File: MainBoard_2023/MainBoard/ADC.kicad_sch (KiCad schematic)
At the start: 6 parts

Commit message: ERC通った
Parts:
- added J12, J13, J14: Conn_01x03, symbol Connector_Generic:Conn_01x03
- gave numbers to parts that had none: 6
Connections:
- net +3.3V: now also J12.1 (Pin_1), J13.1 (Pin_1), J14.1 (Pin_1)
- net GND: now also J12.2 (Pin_2), J13.2 (Pin_2), J14.2 (Pin_2)
- net at IC2.10 (AIN1): now also J14.3 (Pin_3)
- net at IC2.6 (AIN3/REFN1): now also J12.3 (Pin_3)
- net at IC2.7 (AIN2): now also J13.3 (Pin_3)

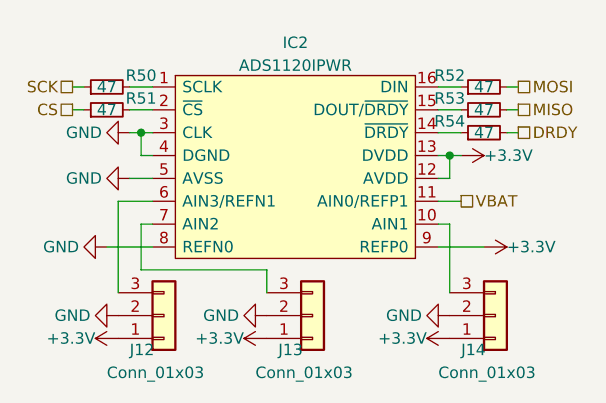
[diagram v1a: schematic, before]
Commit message: フットプリントをすべて割り当て
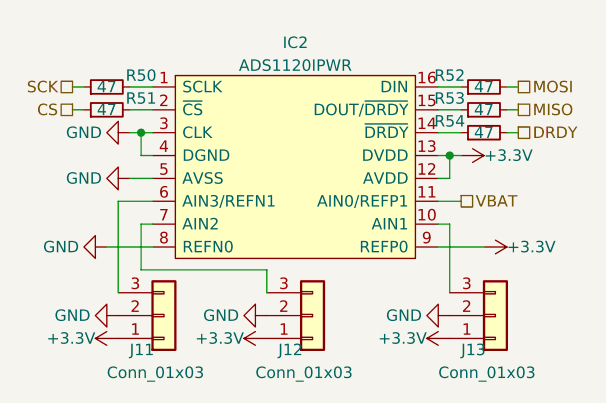
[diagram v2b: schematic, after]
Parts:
- IC2: footprint SOP65P640X120-16N -> ADS1120IPWR:ADS1120IPWR
- J11: renamed from J12; footprint (none) -> B03B-PASK-1:B03B-PASK-1
- J12: renamed from J13; footprint (none) -> B03B-PASK-1:B03B-PASK-1
- J13: renamed from J14; footprint (none) -> B03B-PASK-1:B03B-PASK-1
- R50, R51, R52, R53, R54: footprint (none) -> Resistor_SMD:R_0603_1608Metric_Pad0.98x0.95mm_HandSolder
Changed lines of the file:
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@@
   (symbol (lib_id "Connector_Generic:Conn_01x03") (at 166.37 110.49 0) (mirror x) (unit 1)
     (in_bom yes) (on_board yes)
-    (property "Reference" "J14" (id 0) (at 162.56 114.3 0)
+    (property "Reference" "J13" (id 0) (at 162.56 114.3 0)
       (effects (font (size 1.27 1.27)) (justify left))
     )
@@
       (effects (font (size 1.27 1.27)) (justify left))
     )
-    (property "Footprint" "" (id 2) (at 166.37 110.49 0)
+    (property "Footprint" "B03B-PASK-1:B03B-PASK-1" (id 2) (at 166.37 110.49 0)
       (effects (font (size 1.27 1.27)) hide)
     )
@@
   (symbol (lib_id "power:+3.3V") (at 165.1 102.87 270) (unit 1)
     (in_bom yes) (on_board yes)
-    (property "Reference" "#PWR0121" (id 0) (at 161.29 102.87 0)
+    (property "Reference" "#PWR0122" (id 0) (at 161.29 102.87 0)
       (effects (font (size 1.27 1.27)) hide)
     )
@@
     (property "Reference" "R53" (id 0) (at 161.29 86.36 90))
     (property "Value" "47" (id 1) (at 165.1 87.63 90))
-    (property "Footprint" "" (id 2) (at 165.1 87.63 0)
+    (property "Footprint" "Resistor_SMD:R_0603_1608Metric_Pad0.98x0.95mm_HandSolder" (id 2) (at 165.1 87.63 0)
       (effects (font (size 1.27 1.27)) hide)
     )
@@
   (symbol (lib_id "Connector_Generic:Conn_01x03") (at 146.05 110.49 0) (mirror x) (unit 1)
     (in_bom yes) (on_board yes)
-    (property "Reference" "J13" (id 0) (at 142.24 114.3 0)
+    (property "Reference" "J12" (id 0) (at 142.24 114.3 0)
       (effects (font (size 1.27 1.27)) (justify left))
     )
@@
       (effects (font (size 1.27 1.27)) (justify left))
     )
-    (property "Footprint" "" (id 2) (at 146.05 110.49 0)
+    (property "Footprint" "B03B-PASK-1:B03B-PASK-1" (id 2) (at 146.05 110.49 0)
       (effects (font (size 1.27 1.27)) hide)
     )
@@
     (property "Reference" "R51" (id 0) (at 127 86.36 90))
     (property "Value" "47" (id 1) (at 123.19 87.63 90))
-    (property "Footprint" "" (id 2) (at 123.19 87.63 0)
+    (property "Footprint" "Resistor_SMD:R_0603_1608Metric_Pad0.98x0.95mm_HandSolder" (id 2) (at 123.19 87.63 0)
       (effects (font (size 1.27 1.27)) hide)
     )
@@
   (symbol (lib_id "power:GND") (at 161.29 110.49 270) (unit 1)
     (in_bom yes) (on_board yes)
-    (property "Reference" "#PWR0118" (id 0) (at 154.94 110.49 0)
+    (property "Reference" "#PWR0119" (id 0) (at 154.94 110.49 0)
       (effects (font (size 1.27 1.27)) hide)
     )
@@
     (property "Reference" "R50" (id 0) (at 127 83.82 90))
     (property "Value" "47" (id 1) (at 123.19 85.09 90))
-    (property "Footprint" "" (id 2) (at 123.19 85.09 0)
+    (property "Footprint" "Resistor_SMD:R_0603_1608Metric_Pad0.98x0.95mm_HandSolder" (id 2) (at 123.19 85.09 0)
       (effects (font (size 1.27 1.27)) hide)
     )
@@
     (property "Reference" "R54" (id 0) (at 161.29 88.9 90))
     (property "Value" "47" (id 1) (at 165.1 90.17 90))
-    (property "Footprint" "" (id 2) (at 165.1 90.17 0)
+    (property "Footprint" "Resistor_SMD:R_0603_1608Metric_Pad0.98x0.95mm_HandSolder" (id 2) (at 165.1 90.17 0)
       (effects (font (size 1.27 1.27)) hide)
     )
@@
     (property "Reference" "R52" (id 0) (at 161.29 83.82 90))
     (property "Value" "47" (id 1) (at 165.1 85.09 90))
-    (property "Footprint" "" (id 2) (at 165.1 85.09 0)
+    (property "Footprint" "Resistor_SMD:R_0603_1608Metric_Pad0.98x0.95mm_HandSolder" (id 2) (at 165.1 85.09 0)
       (effects (font (size 1.27 1.27)) hide)
     )
@@
   (symbol (lib_id "power:GND") (at 125.73 95.25 270) (unit 1)
     (in_bom yes) (on_board yes)
-    (property "Reference" "#PWR0115" (id 0) (at 119.38 95.25 0)
+    (property "Reference" "#PWR0116" (id 0) (at 119.38 95.25 0)
       (effects (font (size 1.27 1.27)) hide)
     )
@@
   (symbol (lib_id "power:+3.3V") (at 140.97 113.03 90) (mirror x) (unit 1)
     (in_bom yes) (on_board yes)
-    (property "Reference" "#PWR0117" (id 0) (at 144.78 113.03 0)
+    (property "Reference" "#PWR0118" (id 0) (at 144.78 113.03 0)
       (effects (font (size 1.27 1.27)) hide)
     )
@@
   (symbol (lib_id "power:GND") (at 124.46 110.49 270) (unit 1)
     (in_bom yes) (on_board yes)
-    (property "Reference" "#PWR0112" (id 0) (at 118.11 110.49 0)
+    (property "Reference" "#PWR0113" (id 0) (at 118.11 110.49 0)
       (effects (font (size 1.27 1.27)) hide)
     )
@@
   (symbol (lib_id "power:GND") (at 123.19 102.87 270) (unit 1)
     (in_bom yes) (on_board yes)
-    (property "Reference" "#PWR0111" (id 0) (at 116.84 102.87 0)
+    (property "Reference" "#PWR0112" (id 0) (at 116.84 102.87 0)
       (effects (font (size 1.27 1.27)) hide)
     )
@@
   (symbol (lib_id "power:+3.3V") (at 124.46 113.03 90) (mirror x) (unit 1)
     (in_bom yes) (on_board yes)
-    (property "Reference" "#PWR0113" (id 0) (at 128.27 113.03 0)
+    (property "Reference" "#PWR0114" (id 0) (at 128.27 113.03 0)
       (effects (font (size 1.27 1.27)) hide)
     )
@@
   (symbol (lib_id "power:+3.3V") (at 162.56 92.71 270) (unit 1)
     (in_bom yes) (on_board yes)
-    (property "Reference" "#PWR0120" (id 0) (at 158.75 92.71 0)
+    (property "Reference" "#PWR0121" (id 0) (at 158.75 92.71 0)
       (effects (font (size 1.27 1.27)) hide)
     )
@@
   (symbol (lib_id "power:+3.3V") (at 161.29 113.03 90) (mirror x) (unit 1)
     (in_bom yes) (on_board yes)
-    (property "Reference" "#PWR0119" (id 0) (at 165.1 113.03 0)
+    (property "Reference" "#PWR0120" (id 0) (at 165.1 113.03 0)
       (effects (font (size 1.27 1.27)) hide)
     )
@@
     (property "Reference" "IC2" (id 0) (at 144.145 80.171 0))
     (property "Value" "ADS1120IPWR" (id 1) (at 144.145 82.7079 0))
-    (property "Footprint" "SOP65P640X120-16N" (id 2) (at 167.64 82.55 0)
+    (property "Footprint" "ADS1120IPWR:ADS1120IPWR" (id 2) (at 167.64 82.55 0)
       (effects (font (size 1.27 1.27)) (justify left) hide)
     )
@@
   (symbol (lib_id "power:GND") (at 140.97 110.49 270) (unit 1)
     (in_bom yes) (on_board yes)
-    (property "Reference" "#PWR0116" (id 0) (at 134.62 110.49 0)
+    (property "Reference" "#PWR0117" (id 0) (at 134.62 110.49 0)
       (effects (font (size 1.27 1.27)) hide)
     )
@@
   (symbol (lib_id "Connector_Generic:Conn_01x03") (at 129.54 110.49 0) (mirror x) (unit 1)
     (in_bom yes) (on_board yes)
-    (property "Reference" "J12" (id 0) (at 125.73 114.3 0)
+    (property "Reference" "J11" (id 0) (at 125.73 114.3 0)
       (effects (font (size 1.27 1.27)) (justify left))
     )
@@
       (effects (font (size 1.27 1.27)) (justify left))
     )
-    (property "Footprint" "" (id 2) (at 129.54 110.49 0)
+    (property "Footprint" "B03B-PASK-1:B03B-PASK-1" (id 2) (at 129.54 110.49 0)
       (effects (font (size 1.27 1.27)) hide)
     )
@@
   (symbol (lib_id "power:GND") (at 125.73 90.17 270) (unit 1)
     (in_bom yes) (on_board yes)
-    (property "Reference" "#PWR0114" (id 0) (at 119.38 90.17 0)
-      (effects (font (size 1.27 1.27)) hide)
-    )
+    (property "Reference" "#PWR0115" (id 0) (at 119.38 90.17 0)
+      (effects (font (size 1.27 1.27)) hide)
+    )

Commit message: 部品配置中　モジュラーコネクタを廃止
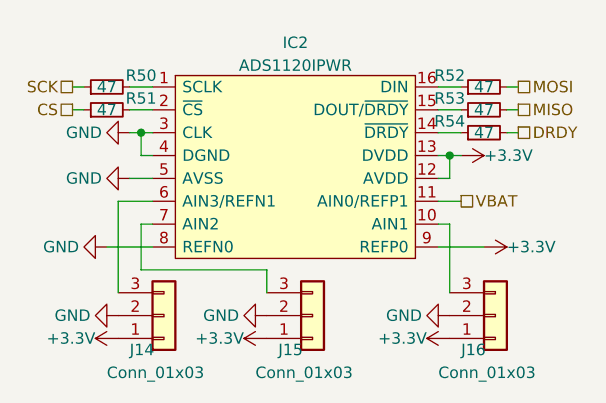
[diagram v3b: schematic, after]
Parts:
- renumbered J11 to J14, J12 to J15, J13 to J16
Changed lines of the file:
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@@
   (symbol (lib_id "Connector_Generic:Conn_01x03") (at 166.37 110.49 0) (mirror x) (unit 1)
     (in_bom yes) (on_board yes)
-    (property "Reference" "J13" (id 0) (at 162.56 114.3 0)
+    (property "Reference" "J16" (id 0) (at 162.56 114.3 0)
       (effects (font (size 1.27 1.27)) (justify left))
     )
@@
   (symbol (lib_id "power:+3.3V") (at 165.1 102.87 270) (unit 1)
     (in_bom yes) (on_board yes)
-    (property "Reference" "#PWR0122" (id 0) (at 161.29 102.87 0)
+    (property "Reference" "#PWR0121" (id 0) (at 161.29 102.87 0)
       (effects (font (size 1.27 1.27)) hide)
     )
@@
   (symbol (lib_id "Connector_Generic:Conn_01x03") (at 146.05 110.49 0) (mirror x) (unit 1)
     (in_bom yes) (on_board yes)
-    (property "Reference" "J12" (id 0) (at 142.24 114.3 0)
+    (property "Reference" "J15" (id 0) (at 142.24 114.3 0)
       (effects (font (size 1.27 1.27)) (justify left))
     )
@@
   (symbol (lib_id "power:GND") (at 161.29 110.49 270) (unit 1)
     (in_bom yes) (on_board yes)
-    (property "Reference" "#PWR0119" (id 0) (at 154.94 110.49 0)
+    (property "Reference" "#PWR0118" (id 0) (at 154.94 110.49 0)
       (effects (font (size 1.27 1.27)) hide)
     )
@@
   (symbol (lib_id "power:GND") (at 125.73 95.25 270) (unit 1)
     (in_bom yes) (on_board yes)
-    (property "Reference" "#PWR0116" (id 0) (at 119.38 95.25 0)
+    (property "Reference" "#PWR0115" (id 0) (at 119.38 95.25 0)
       (effects (font (size 1.27 1.27)) hide)
     )
@@
   (symbol (lib_id "power:+3.3V") (at 140.97 113.03 90) (mirror x) (unit 1)
     (in_bom yes) (on_board yes)
-    (property "Reference" "#PWR0118" (id 0) (at 144.78 113.03 0)
+    (property "Reference" "#PWR0117" (id 0) (at 144.78 113.03 0)
       (effects (font (size 1.27 1.27)) hide)
     )
@@
   (symbol (lib_id "power:GND") (at 124.46 110.49 270) (unit 1)
     (in_bom yes) (on_board yes)
-    (property "Reference" "#PWR0113" (id 0) (at 118.11 110.49 0)
+    (property "Reference" "#PWR0112" (id 0) (at 118.11 110.49 0)
       (effects (font (size 1.27 1.27)) hide)
     )
@@
   (symbol (lib_id "power:GND") (at 123.19 102.87 270) (unit 1)
     (in_bom yes) (on_board yes)
-    (property "Reference" "#PWR0112" (id 0) (at 116.84 102.87 0)
+    (property "Reference" "#PWR0111" (id 0) (at 116.84 102.87 0)
       (effects (font (size 1.27 1.27)) hide)
     )
@@
   (symbol (lib_id "power:+3.3V") (at 124.46 113.03 90) (mirror x) (unit 1)
     (in_bom yes) (on_board yes)
-    (property "Reference" "#PWR0114" (id 0) (at 128.27 113.03 0)
+    (property "Reference" "#PWR0113" (id 0) (at 128.27 113.03 0)
       (effects (font (size 1.27 1.27)) hide)
     )
@@
   (symbol (lib_id "power:+3.3V") (at 162.56 92.71 270) (unit 1)
     (in_bom yes) (on_board yes)
-    (property "Reference" "#PWR0121" (id 0) (at 158.75 92.71 0)
+    (property "Reference" "#PWR0120" (id 0) (at 158.75 92.71 0)
       (effects (font (size 1.27 1.27)) hide)
     )
@@
   (symbol (lib_id "power:+3.3V") (at 161.29 113.03 90) (mirror x) (unit 1)
     (in_bom yes) (on_board yes)
-    (property "Reference" "#PWR0120" (id 0) (at 165.1 113.03 0)
+    (property "Reference" "#PWR0119" (id 0) (at 165.1 113.03 0)
       (effects (font (size 1.27 1.27)) hide)
     )
@@
   (symbol (lib_id "power:GND") (at 140.97 110.49 270) (unit 1)
     (in_bom yes) (on_board yes)
-    (property "Reference" "#PWR0117" (id 0) (at 134.62 110.49 0)
+    (property "Reference" "#PWR0116" (id 0) (at 134.62 110.49 0)
       (effects (font (size 1.27 1.27)) hide)
     )
@@
   (symbol (lib_id "Connector_Generic:Conn_01x03") (at 129.54 110.49 0) (mirror x) (unit 1)
     (in_bom yes) (on_board yes)
-    (property "Reference" "J11" (id 0) (at 125.73 114.3 0)
+    (property "Reference" "J14" (id 0) (at 125.73 114.3 0)
       (effects (font (size 1.27 1.27)) (justify left))
     )
@@
   (symbol (lib_id "power:GND") (at 125.73 90.17 270) (unit 1)
     (in_bom yes) (on_board yes)
-    (property "Reference" "#PWR0115" (id 0) (at 119.38 90.17 0)
-      (effects (font (size 1.27 1.27)) hide)
-    )
+    (property "Reference" "#PWR0114" (id 0) (at 119.38 90.17 0)
+      (effects (font (size 1.27 1.27)) hide)
+    )

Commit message: 回路図とPCBを変更
RJコネクタに変更
秋月のBNO055に変更
気圧センサのフットプリントを変更
ブロックタイプエミフィルのパッドを縮小
外形と取り付け穴を設定
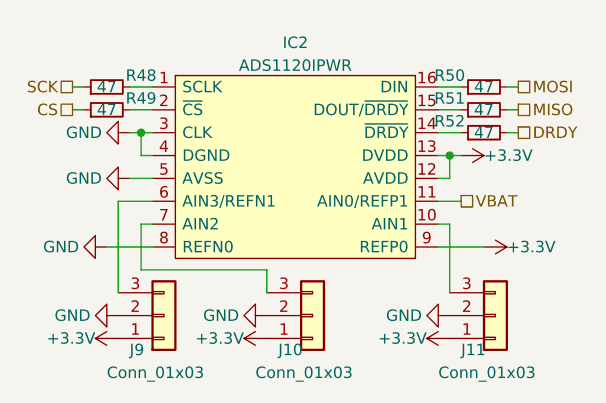
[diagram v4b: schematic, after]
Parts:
- renumbered J15 to J10, J16 to J11, J14 to J9, R50 to R48, R51 to R49, R52 to R50, R53 to R51, R54 to R52
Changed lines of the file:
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@@
   (symbol (lib_id "Connector_Generic:Conn_01x03") (at 166.37 110.49 0) (mirror x) (unit 1)
     (in_bom yes) (on_board yes)
-    (property "Reference" "J16" (id 0) (at 162.56 114.3 0)
+    (property "Reference" "J11" (id 0) (at 162.56 114.3 0)
       (effects (font (size 1.27 1.27)) (justify left))
     )
@@
   (symbol (lib_id "power:+3.3V") (at 165.1 102.87 270) (unit 1)
     (in_bom yes) (on_board yes)
-    (property "Reference" "#PWR0121" (id 0) (at 161.29 102.87 0)
+    (property "Reference" "#PWR0136" (id 0) (at 161.29 102.87 0)
       (effects (font (size 1.27 1.27)) hide)
     )
@@
   (symbol (lib_id "Device:R_Small") (at 165.1 87.63 90) (unit 1)
     (in_bom yes) (on_board yes)
-    (property "Reference" "R53" (id 0) (at 161.29 86.36 90))
+    (property "Reference" "R51" (id 0) (at 161.29 86.36 90))
     (property "Value" "47" (id 1) (at 165.1 87.63 90))
     (property "Footprint" "Resistor_SMD:R_0603_1608Metric_Pad0.98x0.95mm_HandSolder" (id 2) (at 165.1 87.63 0)
@@
   (symbol (lib_id "Connector_Generic:Conn_01x03") (at 146.05 110.49 0) (mirror x) (unit 1)
     (in_bom yes) (on_board yes)
-    (property "Reference" "J15" (id 0) (at 142.24 114.3 0)
+    (property "Reference" "J10" (id 0) (at 142.24 114.3 0)
       (effects (font (size 1.27 1.27)) (justify left))
     )
@@
   (symbol (lib_id "Device:R_Small") (at 123.19 87.63 90) (unit 1)
     (in_bom yes) (on_board yes)
-    (property "Reference" "R51" (id 0) (at 127 86.36 90))
+    (property "Reference" "R49" (id 0) (at 127 86.36 90))
     (property "Value" "47" (id 1) (at 123.19 87.63 90))
     (property "Footprint" "Resistor_SMD:R_0603_1608Metric_Pad0.98x0.95mm_HandSolder" (id 2) (at 123.19 87.63 0)
@@
   (symbol (lib_id "power:GND") (at 161.29 110.49 270) (unit 1)
     (in_bom yes) (on_board yes)
-    (property "Reference" "#PWR0118" (id 0) (at 154.94 110.49 0)
+    (property "Reference" "#PWR0133" (id 0) (at 154.94 110.49 0)
       (effects (font (size 1.27 1.27)) hide)
     )
@@
   (symbol (lib_id "Device:R_Small") (at 123.19 85.09 90) (unit 1)
     (in_bom yes) (on_board yes)
-    (property "Reference" "R50" (id 0) (at 127 83.82 90))
+    (property "Reference" "R48" (id 0) (at 127 83.82 90))
     (property "Value" "47" (id 1) (at 123.19 85.09 90))
     (property "Footprint" "Resistor_SMD:R_0603_1608Metric_Pad0.98x0.95mm_HandSolder" (id 2) (at 123.19 85.09 0)
@@
   (symbol (lib_id "Device:R_Small") (at 165.1 90.17 90) (unit 1)
     (in_bom yes) (on_board yes)
-    (property "Reference" "R54" (id 0) (at 161.29 88.9 90))
+    (property "Reference" "R52" (id 0) (at 161.29 88.9 90))
     (property "Value" "47" (id 1) (at 165.1 90.17 90))
     (property "Footprint" "Resistor_SMD:R_0603_1608Metric_Pad0.98x0.95mm_HandSolder" (id 2) (at 165.1 90.17 0)
@@
   (symbol (lib_id "Device:R_Small") (at 165.1 85.09 90) (unit 1)
     (in_bom yes) (on_board yes)
-    (property "Reference" "R52" (id 0) (at 161.29 83.82 90))
+    (property "Reference" "R50" (id 0) (at 161.29 83.82 90))
     (property "Value" "47" (id 1) (at 165.1 85.09 90))
     (property "Footprint" "Resistor_SMD:R_0603_1608Metric_Pad0.98x0.95mm_HandSolder" (id 2) (at 165.1 85.09 0)
@@
   (symbol (lib_id "power:GND") (at 125.73 95.25 270) (unit 1)
     (in_bom yes) (on_board yes)
-    (property "Reference" "#PWR0115" (id 0) (at 119.38 95.25 0)
+    (property "Reference" "#PWR0130" (id 0) (at 119.38 95.25 0)
       (effects (font (size 1.27 1.27)) hide)
     )
@@
   (symbol (lib_id "power:+3.3V") (at 140.97 113.03 90) (mirror x) (unit 1)
     (in_bom yes) (on_board yes)
-    (property "Reference" "#PWR0117" (id 0) (at 144.78 113.03 0)
+    (property "Reference" "#PWR0132" (id 0) (at 144.78 113.03 0)
       (effects (font (size 1.27 1.27)) hide)
     )
@@
   (symbol (lib_id "power:GND") (at 124.46 110.49 270) (unit 1)
     (in_bom yes) (on_board yes)
-    (property "Reference" "#PWR0112" (id 0) (at 118.11 110.49 0)
+    (property "Reference" "#PWR0127" (id 0) (at 118.11 110.49 0)
       (effects (font (size 1.27 1.27)) hide)
     )
@@
   (symbol (lib_id "power:GND") (at 123.19 102.87 270) (unit 1)
     (in_bom yes) (on_board yes)
-    (property "Reference" "#PWR0111" (id 0) (at 116.84 102.87 0)
+    (property "Reference" "#PWR0126" (id 0) (at 116.84 102.87 0)
       (effects (font (size 1.27 1.27)) hide)
     )
@@
   (symbol (lib_id "power:+3.3V") (at 124.46 113.03 90) (mirror x) (unit 1)
     (in_bom yes) (on_board yes)
-    (property "Reference" "#PWR0113" (id 0) (at 128.27 113.03 0)
+    (property "Reference" "#PWR0128" (id 0) (at 128.27 113.03 0)
       (effects (font (size 1.27 1.27)) hide)
     )
@@
   (symbol (lib_id "power:+3.3V") (at 162.56 92.71 270) (unit 1)
     (in_bom yes) (on_board yes)
-    (property "Reference" "#PWR0120" (id 0) (at 158.75 92.71 0)
+    (property "Reference" "#PWR0135" (id 0) (at 158.75 92.71 0)
       (effects (font (size 1.27 1.27)) hide)
     )
@@
   (symbol (lib_id "power:+3.3V") (at 161.29 113.03 90) (mirror x) (unit 1)
     (in_bom yes) (on_board yes)
-    (property "Reference" "#PWR0119" (id 0) (at 165.1 113.03 0)
+    (property "Reference" "#PWR0134" (id 0) (at 165.1 113.03 0)
       (effects (font (size 1.27 1.27)) hide)
     )
@@
   (symbol (lib_id "power:GND") (at 140.97 110.49 270) (unit 1)
     (in_bom yes) (on_board yes)
-    (property "Reference" "#PWR0116" (id 0) (at 134.62 110.49 0)
+    (property "Reference" "#PWR0131" (id 0) (at 134.62 110.49 0)
       (effects (font (size 1.27 1.27)) hide)
     )
@@
   (symbol (lib_id "Connector_Generic:Conn_01x03") (at 129.54 110.49 0) (mirror x) (unit 1)
     (in_bom yes) (on_board yes)
-    (property "Reference" "J14" (id 0) (at 125.73 114.3 0)
+    (property "Reference" "J9" (id 0) (at 125.73 114.3 0)
       (effects (font (size 1.27 1.27)) (justify left))
     )
@@
   (symbol (lib_id "power:GND") (at 125.73 90.17 270) (unit 1)
     (in_bom yes) (on_board yes)
-    (property "Reference" "#PWR0114" (id 0) (at 119.38 90.17 0)
-      (effects (font (size 1.27 1.27)) hide)
-    )
+    (property "Reference" "#PWR0129" (id 0) (at 119.38 90.17 0)
+      (effects (font (size 1.27 1.27)) hide)
+    )

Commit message: シルクを整えた
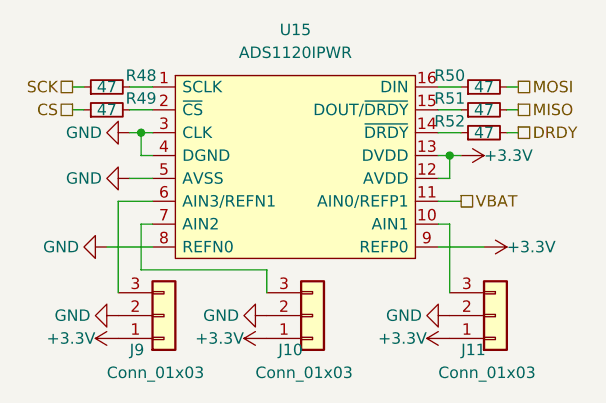
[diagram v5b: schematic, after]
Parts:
- renumbered IC2 to U15
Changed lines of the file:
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@@
   (symbol (lib_id "ADS1120IPWR:ADS1120IPWR") (at 128.27 85.09 0) (unit 1)
     (in_bom yes) (on_board yes) (fields_autoplaced)
-    (property "Reference" "IC2" (id 0) (at 144.145 80.171 0))
-    (property "Value" "ADS1120IPWR" (id 1) (at 144.145 82.7079 0))
+    (property "Reference" "U15" (id 0) (at 144.145 78.74 0))
+    (property "Value" "ADS1120IPWR" (id 1) (at 144.145 81.28 0))
     (property "Footprint" "ADS1120IPWR:ADS1120IPWR" (id 2) (at 167.64 82.55 0)
       (effects (font (size 1.27 1.27)) (justify left) hide)
